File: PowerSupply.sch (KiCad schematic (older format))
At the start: 12 parts, among them CON1 DC_IN, U1 7805

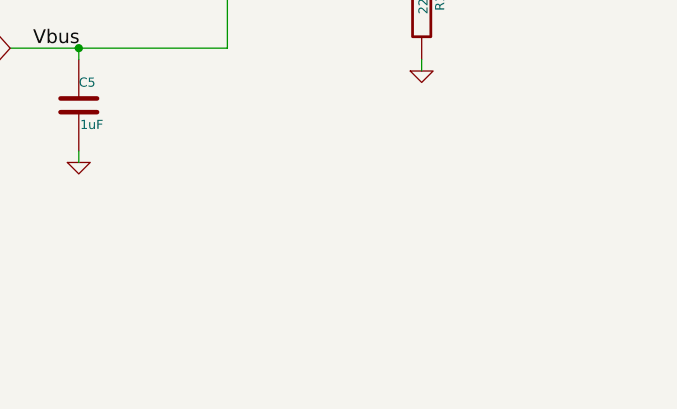
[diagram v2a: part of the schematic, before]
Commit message: Changed the board to use 3.3v rather than 5v. Total new layout.
Since the FTDI chip cannot communicate with the 5v PIC. So run
the PIC at 3.3v This limits the maximum crystal frequency of
the pic, but 4MHz is fine. the internal usb regulator is no
longer used and is replaced with the external one.

The 3.3v regulator get it's 5v from the selected 5v source.
5v is still used by the FTDI chip and the Motor driver.

Signed-off-by: Kolijn Wolfaardt <kolijn.wolfaardt@gmail.com>
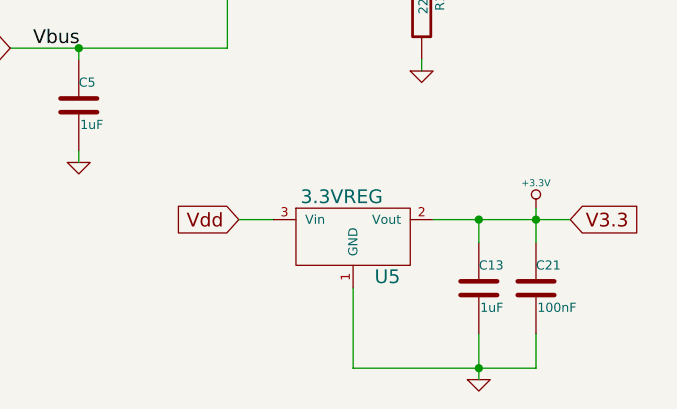
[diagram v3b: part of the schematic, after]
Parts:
- added C13: 1uF, ~, symbol C
- added C21: 100nF, ~, symbol C
- added U5: 3.3VREG, ~, symbol 3.3VREG
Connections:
- net +5V: now also U5.3 (Vin)
- net GND: now also C13.2, C21.2, U5.1 (GND)
- new net +3.3V: C13.1, C21.1, U5.2 (Vout)
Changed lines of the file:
@@
 LIBS:l293
 LIBS:FT230x
+LIBS:33vReg
 LIBS:Robotics Board-cache
 EELAYER 27 0
@@
 Sheet 2 6
 Title ""
-Date "19 apr 2014"
+Date "20 apr 2014"
 Rev ""
 Comp ""
@@
 Wire Wire Line
 	6400 3550 6400 3650
+$Comp
+L C C13
+U 1 1 5353742F
+P 8400 5600
+F 0 "C13" H 8400 5700 40  0000 L CNN
+F 1 "1uF" H 8406 5515 40  0000 L CNN
+F 2 "~" H 8438 5450 30  0000 C CNN
+F 3 "~" H 8400 5600 60  0000 C CNN
+	1    8400 5600
+	1    0    0    -1
+$EndComp
+$Comp
+L C C21
+U 1 1 53537435
+P 8650 5600
+F 0 "C21" H 8650 5700 40  0000 L CNN
+F 1 "100nF" H 8656 5515 40  0000 L CNN
+F 2 "~" H 8688 5450 30  0000 C CNN
+F 3 "~" H 8650 5600 60  0000 C CNN
+	1    8650 5600
+	1    0    0    -1
+$EndComp
+Wire Wire Line
+	8200 5300 8800 5300
+Wire Wire Line
+	8400 5300 8400 5400
+Wire Wire Line
+	7850 5950 8650 5950
+Wire Wire Line
+	8400 5800 8400 6000
+Wire Wire Line
+	8650 5950 8650 5800
+Connection ~ 8400 5950
+Wire Wire Line
+	8650 5250 8650 5400
+Connection ~ 8400 5300
+$Comp
+L GND #PWR08
+U 1 1 53537546
+P 8400 6000
+F 0 "#PWR08" H 8400 6000 30  0001 C CNN
+F 1 "GND" H 8400 5930 30  0001 C CNN
+F 2 "" H 8400 6000 60  0000 C CNN
+F 3 "" H 8400 6000 60  0000 C CNN
+	1    8400 6000
+	1    0    0    -1
+$EndComp
+$Comp
+L +3.3V #PWR09
+U 1 1 53537584
+P 8650 5250
+F 0 "#PWR09" H 8650 5210 30  0001 C CNN
+F 1 "+3.3V" H 8650 5360 30  0000 C CNN
+F 2 "" H 8650 5250 60  0000 C CNN
+F 3 "" H 8650 5250 60  0000 C CNN
+	1    8650 5250
+	1    0    0    -1
+$EndComp
+Connection ~ 8650 5300
+Text GLabel 7350 5300 0    60   Input ~ 0
+Vdd
+Wire Wire Line
+	7350 5300 7500 5300
+Text GLabel 8800 5300 2    60   Input ~ 0
+V3.3
+$Comp
+L 3.3VREG U5
+U 1 1 535376D9
+P 7850 5300
+F 0 "U5" H 8000 5050 60  0000 C CNN
+F 1 "3.3VREG" H 7800 5400 60  0000 C CNN
+F 2 "~" H 7850 5300 60  0000 C CNN
+F 3 "~" H 7850 5300 60  0000 C CNN
+	1    7850 5300
+	1    0    0    -1
+$EndComp
+Wire Wire Line
+	7850 5950 7850 5600
 $EndSCHEMATC
